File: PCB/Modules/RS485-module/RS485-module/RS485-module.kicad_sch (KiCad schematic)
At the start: 8 parts, among them U1 THVD1400D

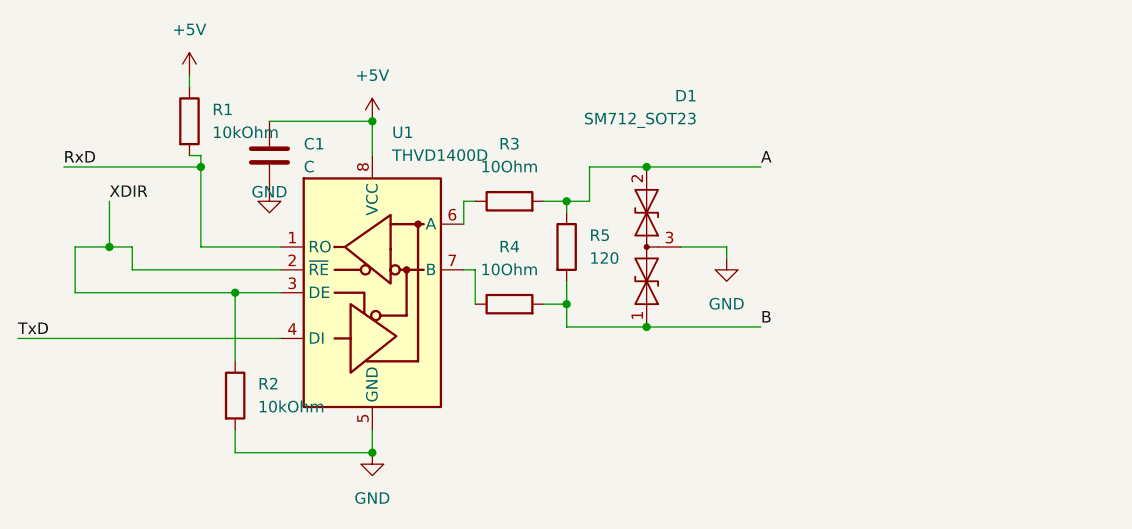
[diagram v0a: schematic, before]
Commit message: Added switch modules and RS485 module
Signed-off-by: Simonca Raul <simonca.raul@gmail.com>
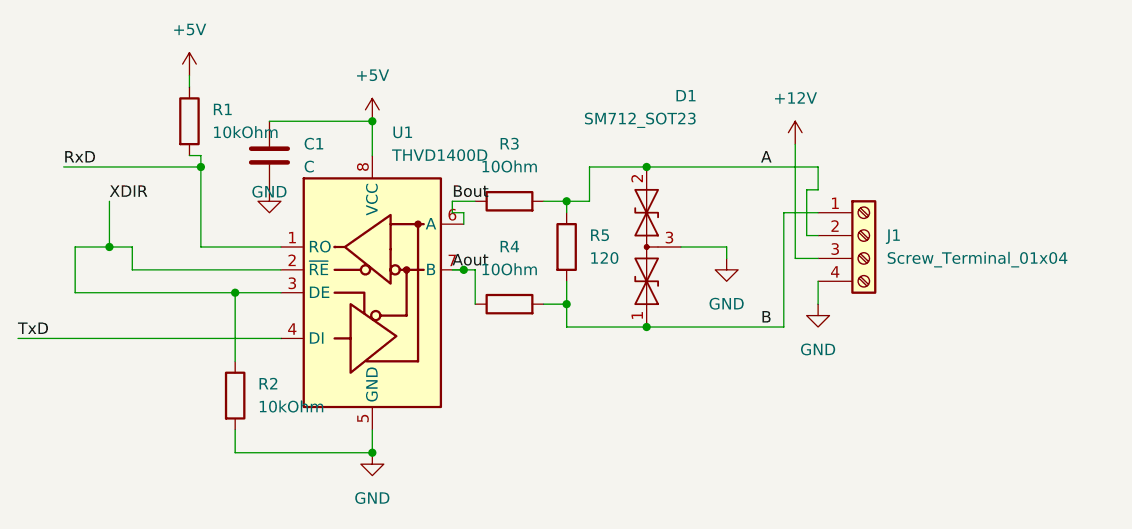
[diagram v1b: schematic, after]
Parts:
- added J1: Screw_Terminal_01x04, TerminalBlock_Altech:Altech_AK100_1x04_P5.00mm, symbol Connector:Screw_Terminal_01x04
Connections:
- net A: now also J1.2 (Pin_2)
- net B: now also J1.1 (Pin_1)
- net GND: now also J1.4 (Pin_4)
- net Aout: now reaches R4.1, U1.7 (B)
- net Bout: now reaches R3.1, U1.6 (A)
- new net +12V: J1.3 (Pin_3)
